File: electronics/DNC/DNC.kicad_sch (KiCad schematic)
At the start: 5 parts

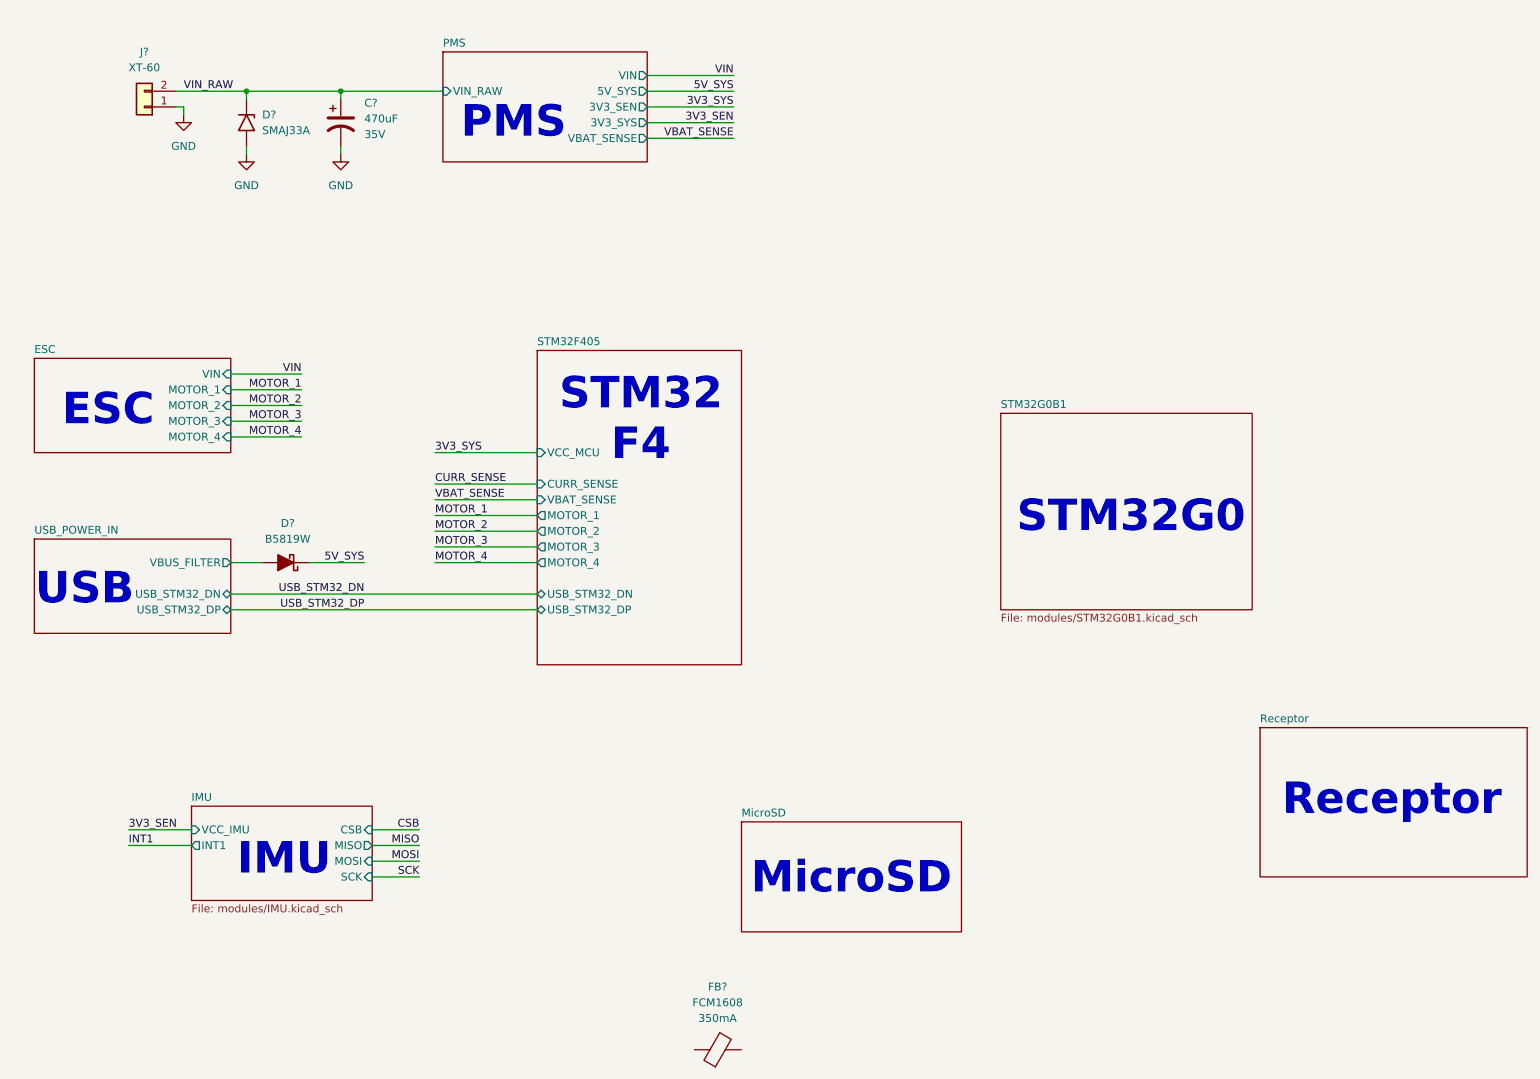
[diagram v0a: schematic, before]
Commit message: Se reemplazó la hoja del IMU por la de sensores y se agregó la hoja de indicadores
- Nueva hoja Sensores: IMU BMI270 (SPI1) y barómetro BMP581 (I2C1 propio, jumper BARO_ADDR).
- Nueva hoja Indicadores: buzzer piezo CPT-12123 con FDV303N y LEDs de estado en PB4/PB5.
- Se eliminó la hoja IMU.
- MicroSD por SDIO de 4 bits con filtro TPD6F002 y TVS ESD5Z3.3 en VDD.
- PMS: AP2112K en 3V3_SYS y LP5907 + ferrita en 3V3_SEN.
- Motores movidos a PA0-PA3 (TIM5) para liberar el SDIO.
- Arquitectura.drawio actualizado a la arquitectura v1 (ELRS por UART, sin OLED).
- Se agregó docs/RESUMEN_PROYECTO_DNC.md con decisiones y pendientes.

Co-Authored-By: Claude Opus 5.5 <noreply@anthropic.com>
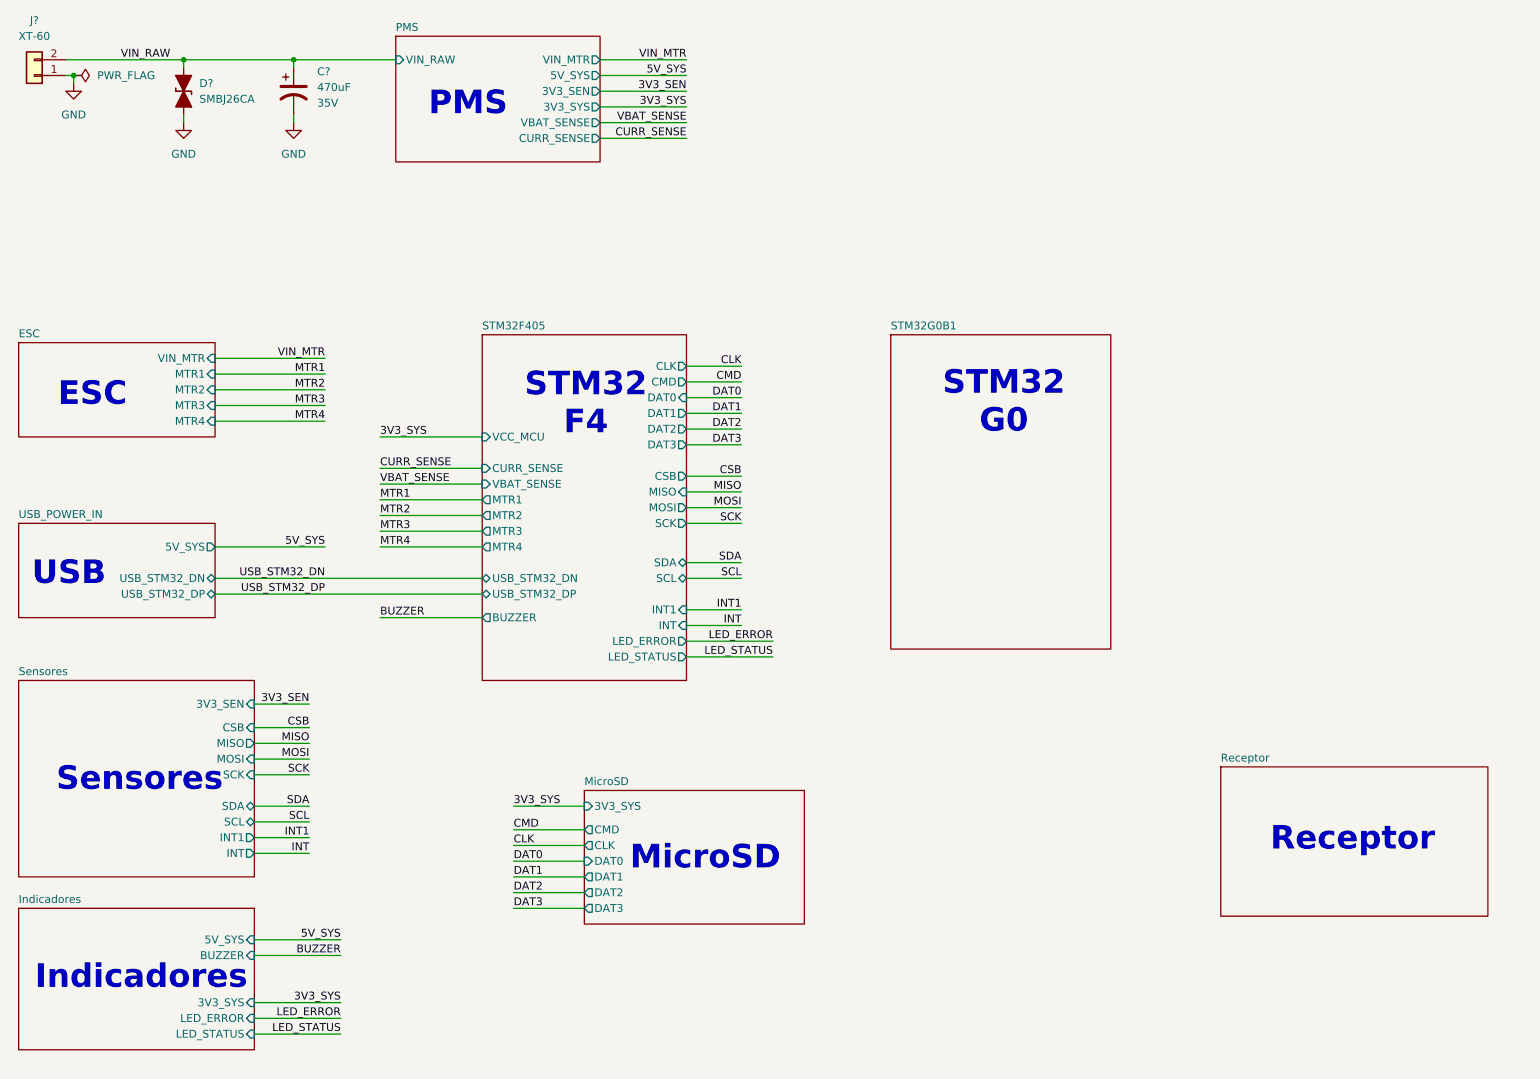
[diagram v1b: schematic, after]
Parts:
- removed D?: B5819W, symbol Device:D_Schottky_Filled
- removed D?: SMAJ33A, Diode_SMD:D_SMA, symbol Diode:SMAJ33A
- removed FB?: FCM1608, Inductor_SMD:L_0603_1608Metric, symbol Device:FerriteBead
- added D?: SMBJ26CA, symbol Device:D_TVS_Filled
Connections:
- net GND: now also D?.1 (A1)
- net VIN_RAW: now also D?.2 (A2)
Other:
- removed sheet IMU
- added sheet Indicadores (modules\Indicadores.kicad_sch)
- added sheet Sensores (modules\Sensores.kicad_sch)
- sheet ESC: file modules\ESC.kicad_sch -> modules/ESC.kicad_sch
- sheet ESC ports: added MTR1, MTR2, MTR3, MTR4, VIN_MTR; removed MOTOR_1, MOTOR_2, MOTOR_3, MOTOR_4, VIN
- sheet MicroSD ports: added 3V3_SYS, CLK, CMD, DAT0, DAT1, DAT2, DAT3; removed none
- sheet PMS: file modules\POWER_MANAGEMENT_SYSTEM.kicad_sch -> modules/POWER_MANAGEMENT_SYSTEM.kicad_sch
- sheet PMS ports: added CURR_SENSE, VIN_MTR; removed VIN
- sheet STM32F405 ports: added BUZZER, CLK, CMD, CSB, DAT0, DAT1, DAT2, DAT3, INT, INT1, LED_ERROR, LED_STATUS, MISO, MOSI, MTR1, MTR2, MTR3, MTR4, SCK, SCL, SDA; removed MOTOR_1, MOTOR_2, MOTOR_3, MOTOR_4
- sheet USB_POWER_IN: file modules\USB_POWER_IN.kicad_sch -> modules/USB_POWER_IN.kicad_sch
- sheet USB_POWER_IN ports: added 5V_SYS; removed VBUS_FILTER
- note added: "Indicadores"
- note added: "STM32 G0"
- note added: "Sensores"
- note removed: "IMU"
- note removed: "STM32G0"
- moved on the sheet: C?, J?

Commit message: Se enlazó el TPS54331 a la librería SJ (SJ_Power:TPS54331DDA)
- PMS: el TPS54331 pasa de DC-DC_Converter (own_symbols) a SJ_Power:TPS54331DDA.
  Netlist verificado: todas las redes iguales; el pad térmico (pin 9, ahora PAD) sigue en GND.
- Indicadores y raíz: cambios menores de KiCad (referencias sin anotar).

Co-Authored-By: Claude Opus 5.5 <noreply@anthropic.com>
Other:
- sheet Indicadores: file modules\Indicadores.kicad_sch -> modules/Indicadores.kicad_sch
- sheet MicroSD: file modules\MicroSD.kicad_sch -> modules/MicroSD.kicad_sch
- sheet Receptor: file modules\Receptor.kicad_sch -> modules/Receptor.kicad_sch
- sheet STM32F405: file modules\STM32F405.kicad_sch -> modules/STM32F405.kicad_sch
- sheet Sensores: file modules\Sensores.kicad_sch -> modules/Sensores.kicad_sch
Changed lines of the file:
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@@
 			)
 		)
-		(property "Sheetfile" "modules\\Indicadores.kicad_sch"
+		(property "Sheetfile" "modules/Indicadores.kicad_sch"
 			(at 26.67 193.6246 0)
 			(hide yes)
@@
 			)
 		)
-		(property "Sheetfile" "modules\\MicroSD.kicad_sch"
+		(property "Sheetfile" "modules/MicroSD.kicad_sch"
 			(at 118.11 173.3046 0)
 			(hide yes)
@@
 			)
 		)
-		(property "Sheetfile" "modules\\Sensores.kicad_sch"
+		(property "Sheetfile" "modules/Sensores.kicad_sch"
 			(at 26.67 165.6846 0)
 			(hide yes)
@@
 			)
 		)
-		(property "Sheetfile" "modules\\Receptor.kicad_sch"
+		(property "Sheetfile" "modules/Receptor.kicad_sch"
 			(at 220.98 172.0346 0)
 			(hide yes)
@@
 			)
 		)
-		(property "Sheetfile" "modules\\STM32F405.kicad_sch"
+		(property "Sheetfile" "modules/STM32F405.kicad_sch"
 			(at 101.6 133.9346 0)
 			(hide yes)

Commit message: XT60 con huella estándar y BMI270 enlazado a SJ_Sensor
- XT60: Gen_devices:AMASS_XT60-M -> Connector_AMASS:AMASS_XT60-M_1x02_P7.20mm_Vertical
  (misma geometría y polaridad: pin 1 GND, pin 2 VIN_RAW), con los campos SJ.
- Sensores: BMI270 pasa de Sensor_Motion:BMI160 a SJ_Sensor:BMI270 (misma geometría;
  netlist idéntico, sin cambios de cableado). Pines sin usar según Bosch: ASDx/ASCx,
  INT2, OCSB y OSDO sin conectar.

Co-Authored-By: Claude Opus 5.5 <noreply@anthropic.com>
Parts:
- J?: footprint Gen_devices:AMASS_XT60-M -> Connector_AMASS:AMASS_XT60-M_1x02_P7.20mm_Vertical
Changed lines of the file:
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@@
 			)
 		)
-		(property "Footprint" "Gen_devices:AMASS_XT60-M"
+		(property "Footprint" "Connector_AMASS:AMASS_XT60-M_1x02_P7.20mm_Vertical"
 			(at 29.21 35.56 0)
 			(hide yes)
@@
 			(show_name no)
 			(do_not_autoplace no)
+			(effects
+				(font
+					(size 1.27 1.27)
+				)
+			)
+		)
+		(property "Manufacturer" ""
+			(at 29.21 35.56 0)
+			(hide yes)
+			(show_name no)
+			(do_not_autoplace no)
+			(effects
+				(font
+					(size 1.27 1.27)
+				)
+			)
+		)
+		(property "Mfg Part #" ""
+			(at 29.21 35.56 0)
+			(hide yes)
+			(show_name no)
+			(do_not_autoplace no)
+			(effects
+				(font
+					(size 1.27 1.27)
+				)
+			)
+		)
+		(property "LCSC Part #" ""
+			(at 29.21 35.56 0)
+			(hide yes)
+			(show_name no)
+			(do_not_autoplace no)
+			(effects
+				(font
+					(size 1.27 1.27)
+				)
+			)
+		)
+		(property "Supplier" ""
+			(at 29.21 35.56 0)
+			(hide yes)
+			(show_name no)
+			(do_not_autoplace no)
+			(effects
+				(font
+					(size 1.27 1.27)
+				)
+			)
+		)
+		(property "Cost" ""
+			(at 29.21 35.56 0)
+			(hide yes)
+			(show_name no)
+			(do_not_autoplace no)
+			(effects
+				(font
+					(size 1.27 1.27)
+				)
+			)
+		)
+		(property "Voltage" ""
+			(at 29.21 35.56 0)
+			(show_name no)
+			(do_not_autoplace no)
+			(effects
+				(font
+					(size 1.27 1.27)
+				)
+			)
+		)
+		(property "Current" ""
+			(at 29.21 35.56 0)
+			(show_name no)
+			(do_not_autoplace no)
+			(effects
+				(font
+					(size 1.27 1.27)
+				)
+			)
+		)
+		(property "TC" ""
+			(at 29.21 35.56 0)
+			(show_name no)
+			(do_not_autoplace no)
+			(effects
+				(font
+					(size 1.27 1.27)
+				)
+			)
+		)
+		(property "Power" ""
+			(at 29.21 35.56 0)
+			(show_name no)
+			(do_not_autoplace no)
+			(effects
+				(font
+					(size 1.27 1.27)
+				)
+			)
+		)
+		(property "Tol" ""
+			(at 29.21 35.56 0)
+			(show_name no)
+			(do_not_autoplace no)

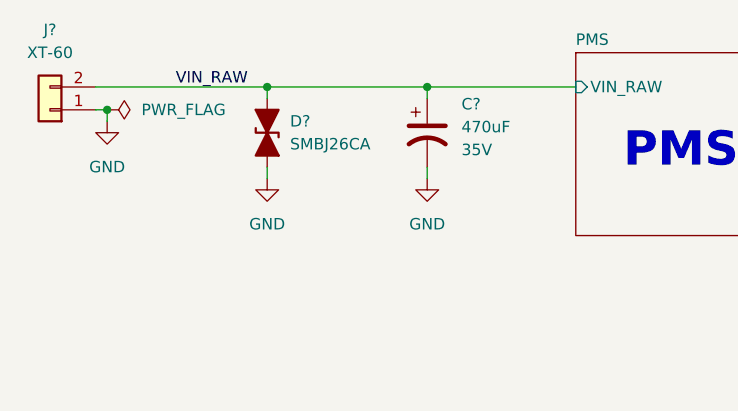
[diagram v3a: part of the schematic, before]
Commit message: Protección de entrada para 4S: TVS SMBJ18A e INA169 alimentado desde 3V3_SYS
- TVS: SMBJ26CA bidireccional (clamp ~42 V) -> SMBJ18A unidireccional (VR 18 V,
  VC 29.2 V @ 20.5 A), por debajo del máximo absoluto de 30 V del TPS54331. Símbolo
  genérico Diode:SM6T18A (misma geometría y familia de 600 W/SMB), huella Diode_SMD:D_SMB;
  cátodo a VIN_RAW.
- INA169: V+ y su desacoplo pasan de 5V_SYS a 3V3_SYS; la salida queda limitada a
  ~(V+ - 0.9 V), así que PB1 (ADC) no puede superar 3.3 V.
- RL 47k -> 27k: 13.5 mV/A, 1.89 V a 140 A (dentro de la salida garantizada). 10 nF en
  paralelo como filtro (~590 Hz).
- MVP1 = 4S. El 6S necesitaría un buck de 60 V; queda pospuesto.

Co-Authored-By: Claude Opus 5.5 <noreply@anthropic.com>
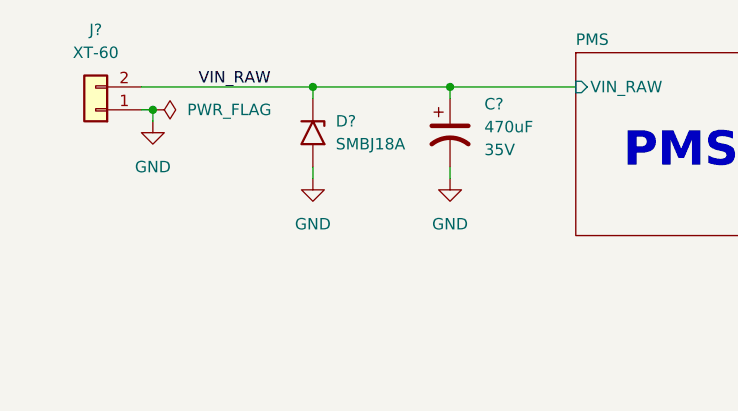
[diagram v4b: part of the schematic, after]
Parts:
- removed D?: SMBJ26CA, symbol Device:D_TVS_Filled
- added D?: SMBJ18A, Diode_SMD:D_SMB, symbol Diode:SM6T18A
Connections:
- net GND: now also D?.2 (A2)
- net VIN_RAW: now also D?.1 (A1)
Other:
- moved on the sheet: C?, J?

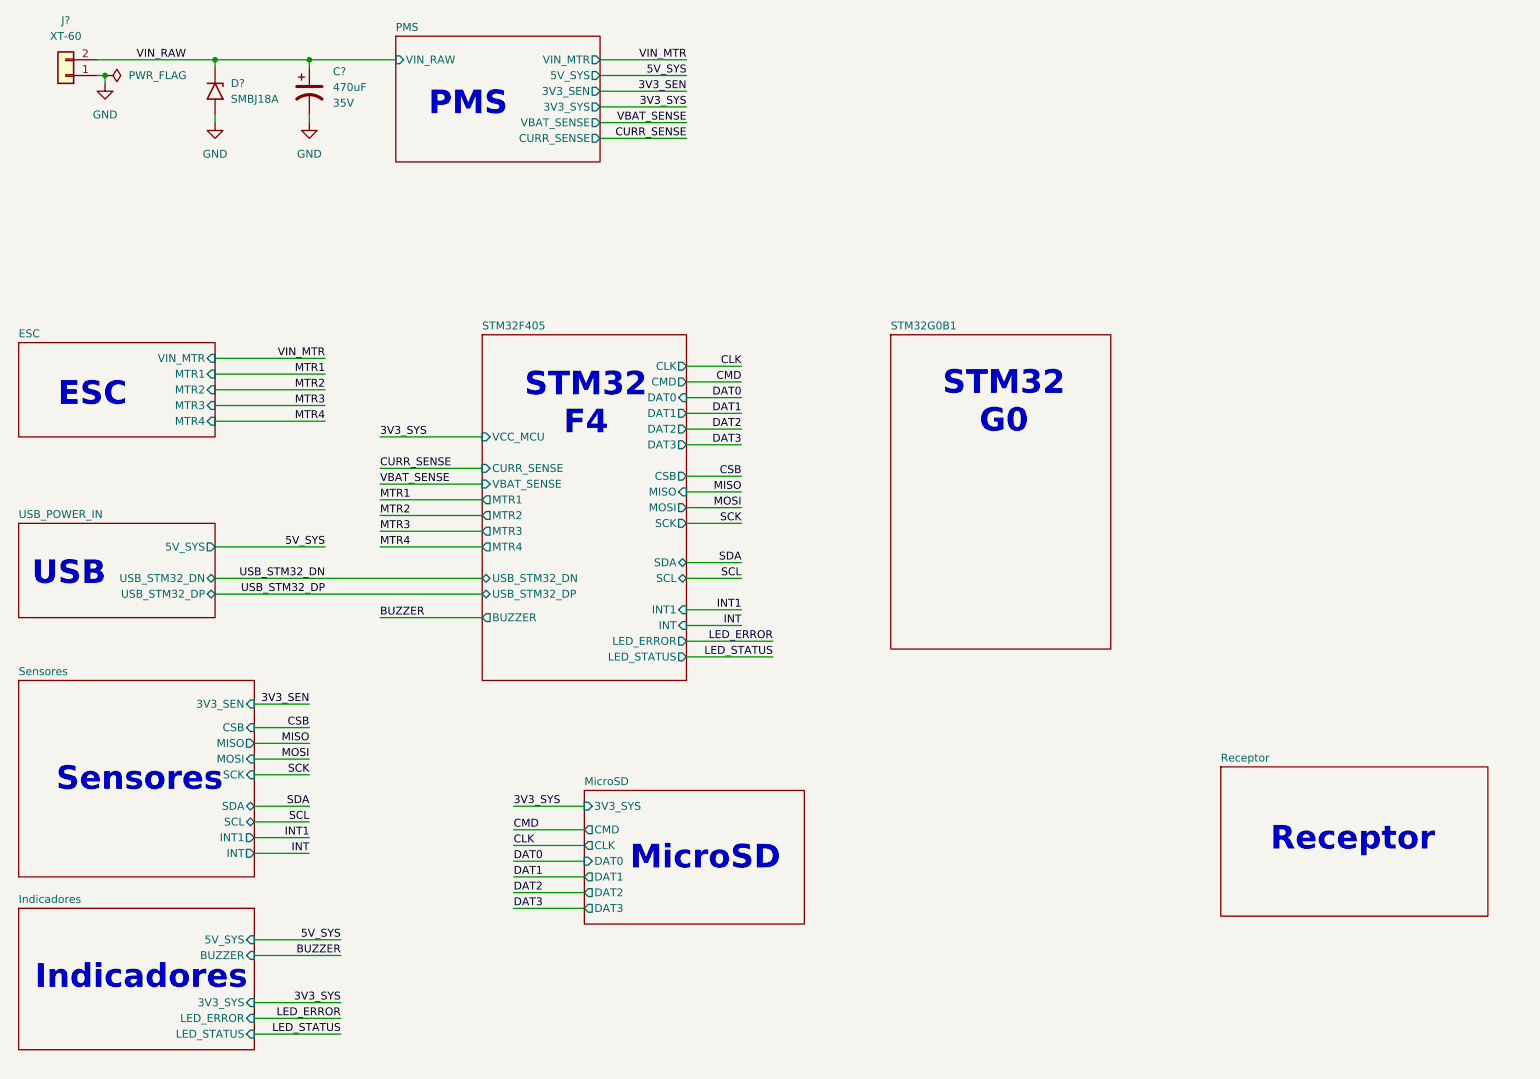
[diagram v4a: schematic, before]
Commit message: Hoja ESC: pads de potencia THT, ESD en las señales MTR y pads de señal/GND
- Por ESC: M12V (VIN_MTR) y MGND (GND) como Conn_01x01 con huella
  Connector_Wire:SolderWire-1.5sqmm_1x01_D1.7mm_OD3.9mm (cable de 16 AWG, ~15 A por ESC en el MVP1);
  señal (MTRx_PAD, tras 220 ohm) y su tierra de referencia (GNDx_PAD) con TestPoint_Pad_2.0x2.0mm.
- ESD IEC 61000-4-2 nivel 4: USBLC6-4SC6 en los 4 pads de señal, VBUS a 3V3_SYS con 100 nF.
- Se eliminan los MountingHole_Pad y la dependencia de Gen_devices en esta hoja.
- Raíz: solo reacomodos gráficos (netlist sin cambios).
- Los huecos de montaje se agregan con el contorno de la placa.

Co-Authored-By: Claude Opus 5.5 <noreply@anthropic.com>
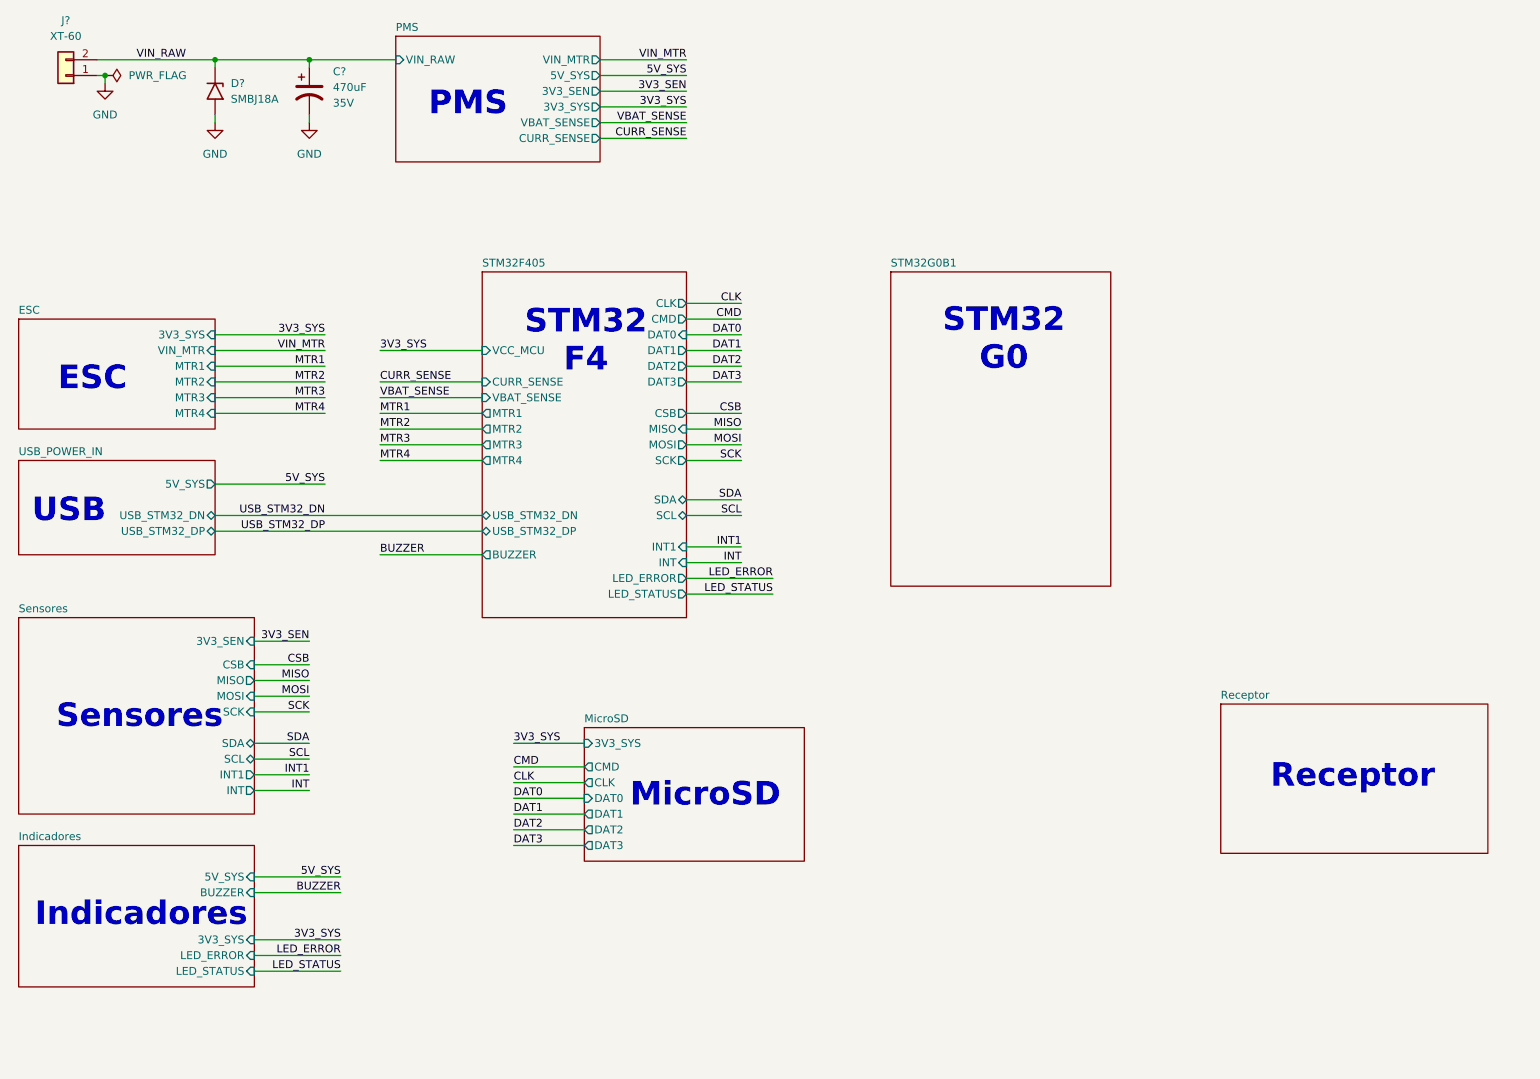
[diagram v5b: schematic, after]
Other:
- sheet ESC ports: added 3V3_SYS; removed none
